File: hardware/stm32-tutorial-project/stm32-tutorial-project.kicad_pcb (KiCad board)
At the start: 2 copper layers, 7 parts, among them J2 10pin IDC SWD, U1 STM32G431CBTx

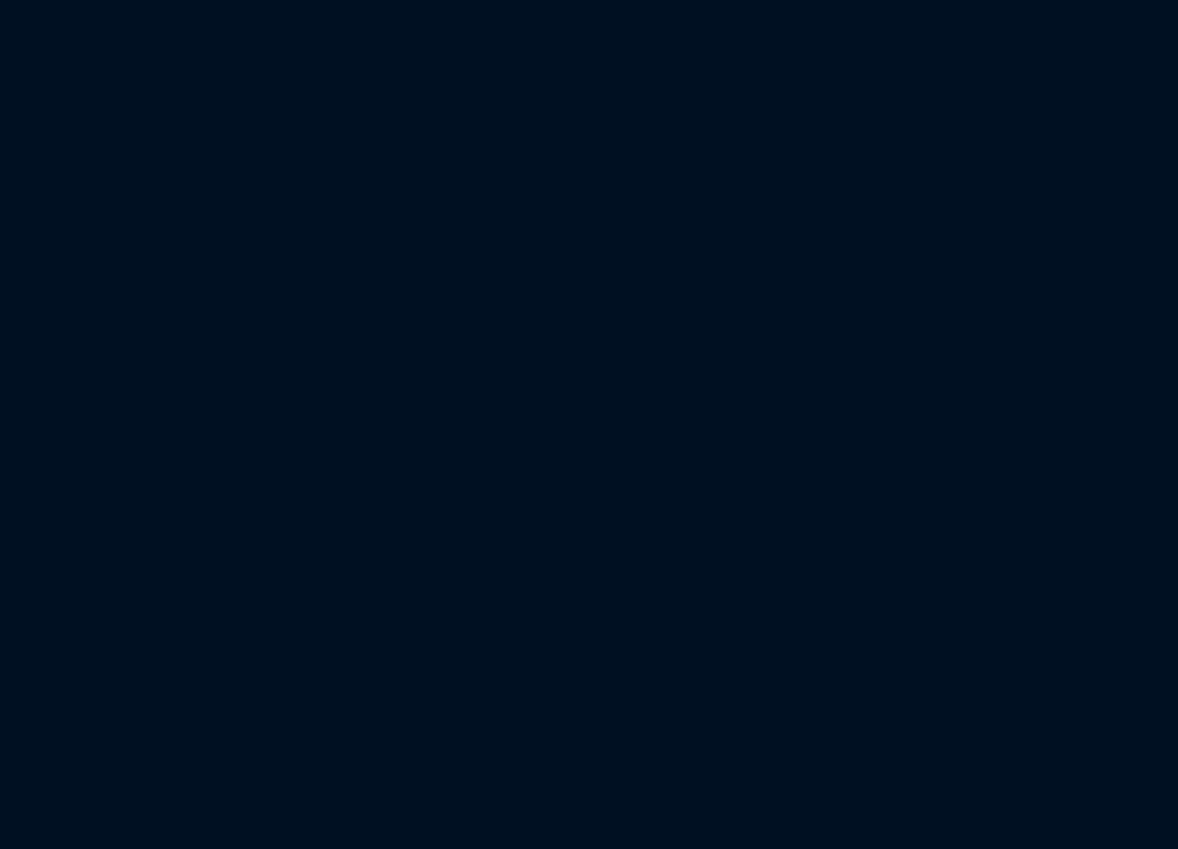
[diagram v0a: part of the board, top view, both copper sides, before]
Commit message: Add missing connectors, test points, and jumpers
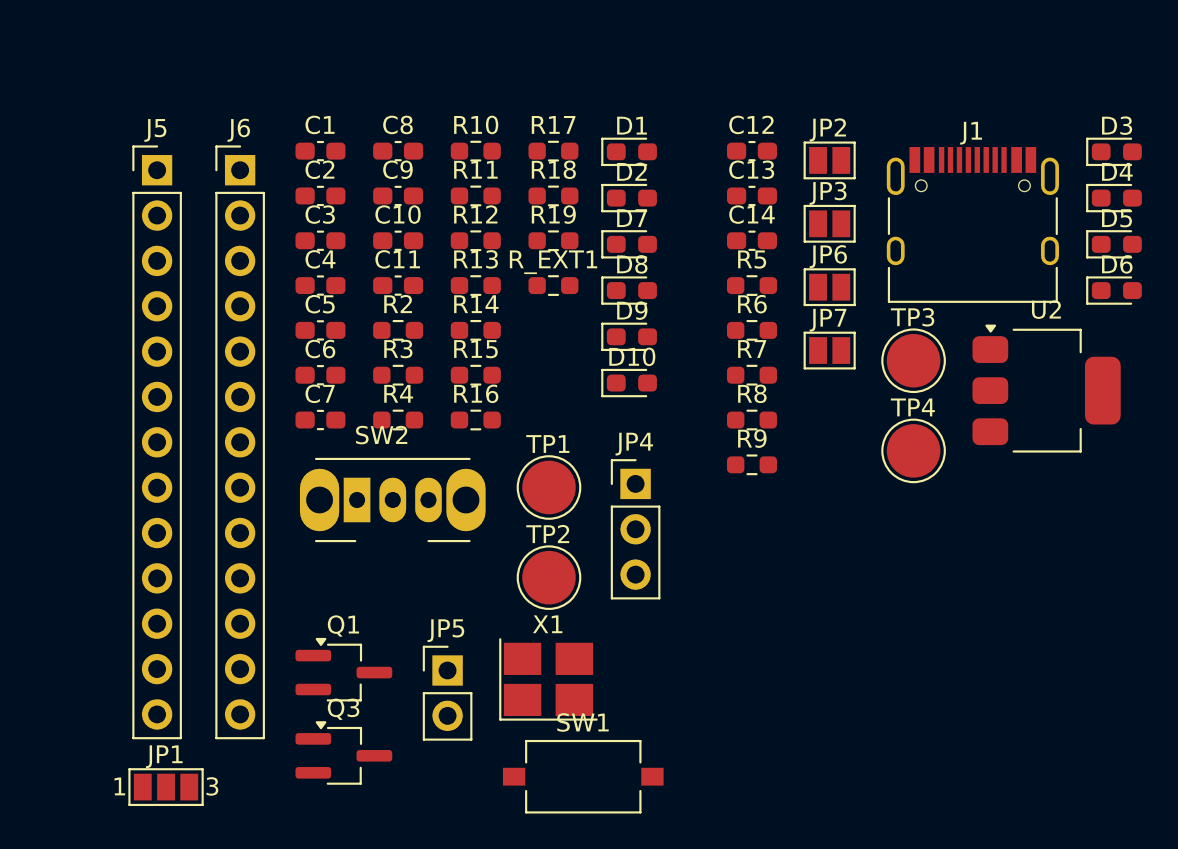
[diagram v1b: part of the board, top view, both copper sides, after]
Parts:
- added C1: 100n, Capacitor_SMD:C_0603_1608Metric_Pad1.08x0.95mm_HandSolder, F.Cu at (164.2, 111.1)
- added C10: 12pf, Capacitor_SMD:C_0603_1608Metric_Pad1.08x0.95mm_HandSolder, F.Cu at (168.5, 116.1)
- added C11: 100n, Capacitor_SMD:C_0603_1608Metric_Pad1.08x0.95mm_HandSolder, F.Cu at (168.5, 118.6)
- added C12: 10u, Capacitor_SMD:C_0603_1608Metric_Pad1.08x0.95mm_HandSolder, F.Cu at (188.3, 111.1)
- added C13: 10u, Capacitor_SMD:C_0603_1608Metric_Pad1.08x0.95mm_HandSolder, F.Cu at (188.3, 113.6)
- added C14: 22u, Capacitor_SMD:C_0603_1608Metric_Pad1.08x0.95mm_HandSolder, F.Cu at (188.3, 116.1)
- added C2: 1u, Capacitor_SMD:C_0603_1608Metric_Pad1.08x0.95mm_HandSolder, F.Cu at (164.2, 113.6)
- added C3: 4.7u, Capacitor_SMD:C_0603_1608Metric_Pad1.08x0.95mm_HandSolder, F.Cu at (164.2, 116.1)
- added C4: 100n, Capacitor_SMD:C_0603_1608Metric_Pad1.08x0.95mm_HandSolder, F.Cu at (164.2, 118.6)
- added C5: 100n, Capacitor_SMD:C_0603_1608Metric_Pad1.08x0.95mm_HandSolder, F.Cu at (164.2, 121.1)
- added C6: 100n, Capacitor_SMD:C_0603_1608Metric_Pad1.08x0.95mm_HandSolder, F.Cu at (164.2, 123.6)
- added C7: 10n, Capacitor_SMD:C_0603_1608Metric_Pad1.08x0.95mm_HandSolder, F.Cu at (164.2, 126.1)
- added C8: 1u, Capacitor_SMD:C_0603_1608Metric_Pad1.08x0.95mm_HandSolder, F.Cu at (168.5, 111.1)
- added C9: 12pf, Capacitor_SMD:C_0603_1608Metric_Pad1.08x0.95mm_HandSolder, F.Cu at (168.5, 113.6)
- added D1: LED, Diode_SMD:D_0603_1608Metric_Pad1.05x0.95mm_HandSolder, F.Cu at (181.6, 111.1)
- added D10: LED, Diode_SMD:D_0603_1608Metric_Pad1.05x0.95mm_HandSolder, F.Cu at (181.6, 124.1)
- added D2: LED, Diode_SMD:D_0603_1608Metric_Pad1.05x0.95mm_HandSolder, F.Cu at (181.6, 113.7)
- added D3: D_Schottky, Diode_SMD:D_0603_1608Metric_Pad1.05x0.95mm_HandSolder, F.Cu at (208.8, 111.1)
- added D4: D_Schottky, Diode_SMD:D_0603_1608Metric_Pad1.05x0.95mm_HandSolder, F.Cu at (208.8, 113.7)
- added D5: LED, Diode_SMD:D_0603_1608Metric_Pad1.05x0.95mm_HandSolder, F.Cu at (208.8, 116.3)
- added D6: LED, Diode_SMD:D_0603_1608Metric_Pad1.05x0.95mm_HandSolder, F.Cu at (208.8, 118.9)
- added D7: LED, Diode_SMD:D_0603_1608Metric_Pad1.05x0.95mm_HandSolder, F.Cu at (181.6, 116.3)
- added D8: LED, Diode_SMD:D_0603_1608Metric_Pad1.05x0.95mm_HandSolder, F.Cu at (181.6, 118.9)
- added D9: LED, Diode_SMD:D_0603_1608Metric_Pad1.05x0.95mm_HandSolder, F.Cu at (181.6, 121.5)
- added J1: USB_C_Receptacle_USB2.0_14P, Connector_USB:USB_C_Receptacle_HRO_TYPE-C-31-M-12, F.Cu at (200.7, 115.6)
- added J5: Conn_01x13, Connector_PinHeader_2.54mm:PinHeader_1x13_P2.54mm_Vertical, F.Cu at (155.0, 112.2)
- added J6: Conn_01x13, Connector_PinHeader_2.54mm:PinHeader_1x13_P2.54mm_Vertical, F.Cu at (159.7, 112.2)
- added JP1: VBAT_SLEC, Jumper:SolderJumper-3_P1.3mm_Open_Pad1.0x1.5mm_NumberLabels, F.Cu at (155.5, 146.7)
- added JP2: 5V_sense, Jumper:SolderJumper-2_P1.3mm_Open_Pad1.0x1.5mm, F.Cu at (192.7, 111.6)
- added JP3: Schottky_bypass, Jumper:SolderJumper-2_P1.3mm_Open_Pad1.0x1.5mm, F.Cu at (192.7, 115.2)
- added JP4: 5V_SLEC, Connector_PinHeader_2.54mm:PinHeader_1x03_P2.54mm_Vertical, F.Cu at (181.8, 129.7)
- added JP5: I2C_PULL_UPS_EN, Connector_PinHeader_2.54mm:PinHeader_1x02_P2.54mm_Vertical, F.Cu at (171.3, 140.2)
- added JP6: REG_OUT, Jumper:SolderJumper-2_P1.3mm_Open_Pad1.0x1.5mm, F.Cu at (192.7, 118.7)
- added JP7: REG_IN, Jumper:SolderJumper-2_P1.3mm_Open_Pad1.0x1.5mm, F.Cu at (192.7, 122.3)
- added Q1: NPN, Package_TO_SOT_SMD:TSOT-23_HandSoldering, F.Cu at (165.5, 140.3)
- added Q3: PNP, Package_TO_SOT_SMD:TSOT-23_HandSoldering, F.Cu at (165.5, 145.0)
- added R10: 500, Resistor_SMD:R_0603_1608Metric_Pad0.98x0.95mm_HandSolder, F.Cu at (172.9, 111.1)
- added R11: 500, Resistor_SMD:R_0603_1608Metric_Pad0.98x0.95mm_HandSolder, F.Cu at (172.9, 113.6)
- added R12: 500, Resistor_SMD:R_0603_1608Metric_Pad0.98x0.95mm_HandSolder, F.Cu at (172.9, 116.1)
- added R13: 1k, Resistor_SMD:R_0603_1608Metric_Pad0.98x0.95mm_HandSolder, F.Cu at (172.9, 118.6)
- added R14: 1k, Resistor_SMD:R_0603_1608Metric_Pad0.98x0.95mm_HandSolder, F.Cu at (172.9, 121.1)
- added R15: 500, Resistor_SMD:R_0603_1608Metric_Pad0.98x0.95mm_HandSolder, F.Cu at (172.9, 123.6)
- added R16: 10k, Resistor_SMD:R_0603_1608Metric_Pad0.98x0.95mm_HandSolder, F.Cu at (172.9, 126.1)
- added R17: 10k, Resistor_SMD:R_0603_1608Metric_Pad0.98x0.95mm_HandSolder, F.Cu at (177.2, 111.1)
- added R18: 4.7k, Resistor_SMD:R_0603_1608Metric_Pad0.98x0.95mm_HandSolder, F.Cu at (177.2, 113.6)
- added R19: 4.7k, Resistor_SMD:R_0603_1608Metric_Pad0.98x0.95mm_HandSolder, F.Cu at (177.2, 116.1)
- added R2: 500, Resistor_SMD:R_0603_1608Metric_Pad0.98x0.95mm_HandSolder, F.Cu at (168.5, 121.1)
- added R3: 10k, Resistor_SMD:R_0603_1608Metric_Pad0.98x0.95mm_HandSolder, F.Cu at (168.5, 123.6)
- added R4: 500, Resistor_SMD:R_0603_1608Metric_Pad0.98x0.95mm_HandSolder, F.Cu at (168.5, 126.1)
- added R5: 0, Resistor_SMD:R_0603_1608Metric_Pad0.98x0.95mm_HandSolder, F.Cu at (188.3, 118.6)
- added R6: 5.1k, Resistor_SMD:R_0603_1608Metric_Pad0.98x0.95mm_HandSolder, F.Cu at (188.3, 121.1)
- added R7: 5.1k, Resistor_SMD:R_0603_1608Metric_Pad0.98x0.95mm_HandSolder, F.Cu at (188.3, 123.6)
- added R8: 500, Resistor_SMD:R_0603_1608Metric_Pad0.98x0.95mm_HandSolder, F.Cu at (188.3, 126.1)
- added R9: 500, Resistor_SMD:R_0603_1608Metric_Pad0.98x0.95mm_HandSolder, F.Cu at (188.3, 128.7)
- added R_EXT1: 0, Resistor_SMD:R_0603_1608Metric_Pad0.98x0.95mm_HandSolder, F.Cu at (177.2, 118.6)
- added SW1: SW_Push, Button_Switch_SMD:SW_Tactile_SPST_NO_Straight_CK_PTS636Sx25SMTRLFS, F.Cu at (178.9, 146.1)
- added SW2: SW_Push_SPDT, Button_Switch_THT:SW_Slide_SPDT_Angled_CK_OS102011MA1Q, F.Cu at (166.2, 130.6)
- added TP1: DIGITAL_IO_1, TestPoint:TestPoint_Pad_D3.0mm, F.Cu at (177.0, 129.9)
- added TP2: DIGITAL_IO_2, TestPoint:TestPoint_Pad_D3.0mm, F.Cu at (177.0, 135.0)
- added TP3: VBUS, TestPoint:TestPoint_Pad_D3.0mm, F.Cu at (197.4, 122.8)
- added TP4: 5V, TestPoint:TestPoint_Pad_D3.0mm, F.Cu at (197.4, 127.9)
- added U2: AZ1117-3.3, Package_TO_SOT_SMD:SOT-223-3_TabPin2, F.Cu at (204.8, 124.5)
- added X1: Crystal_GND24, Crystal:Crystal_SMD_3225-4Pin_3.2x2.5mm_HandSoldering, F.Cu at (176.9, 140.7)
- D11: value SP0504BAHT -> SP0504BAHTG

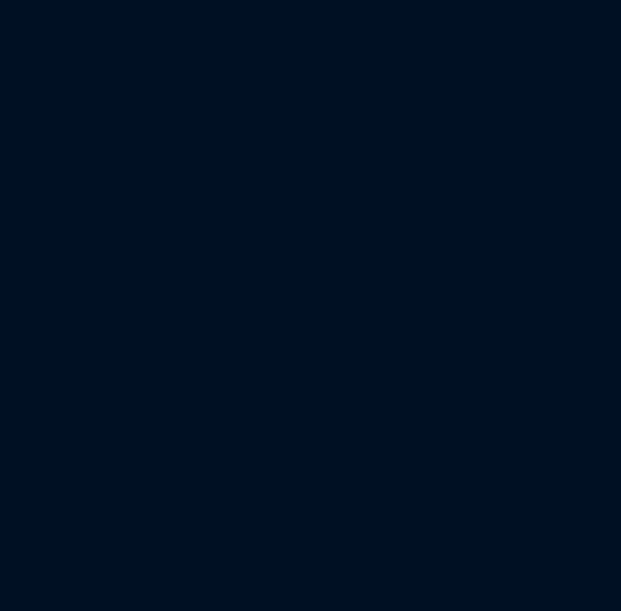
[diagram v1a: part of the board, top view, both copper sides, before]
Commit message: Correct remaining connectors, complete ratsnest now available
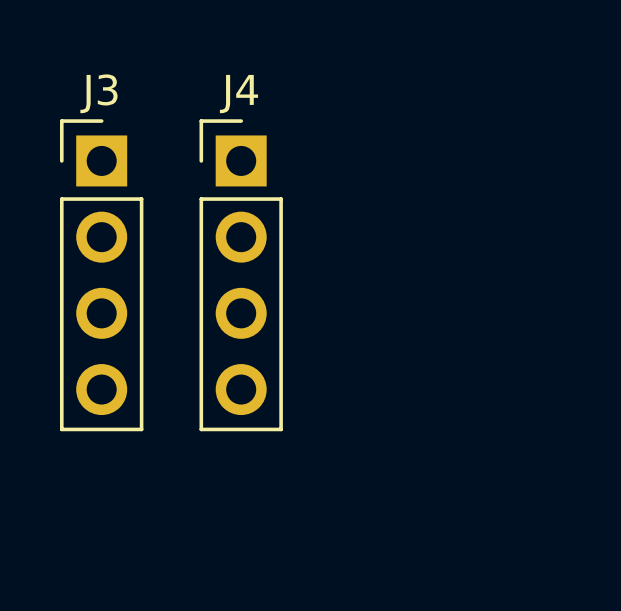
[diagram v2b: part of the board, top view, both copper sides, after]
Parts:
- added J3: Conn_01x04, Connector_PinHeader_2.54mm:PinHeader_1x04_P2.54mm_Vertical, F.Cu at (105.3, 77.4)
- added J4: Conn_01x04, Connector_PinHeader_2.54mm:PinHeader_1x04_P2.54mm_Vertical, F.Cu at (110.0, 77.4)

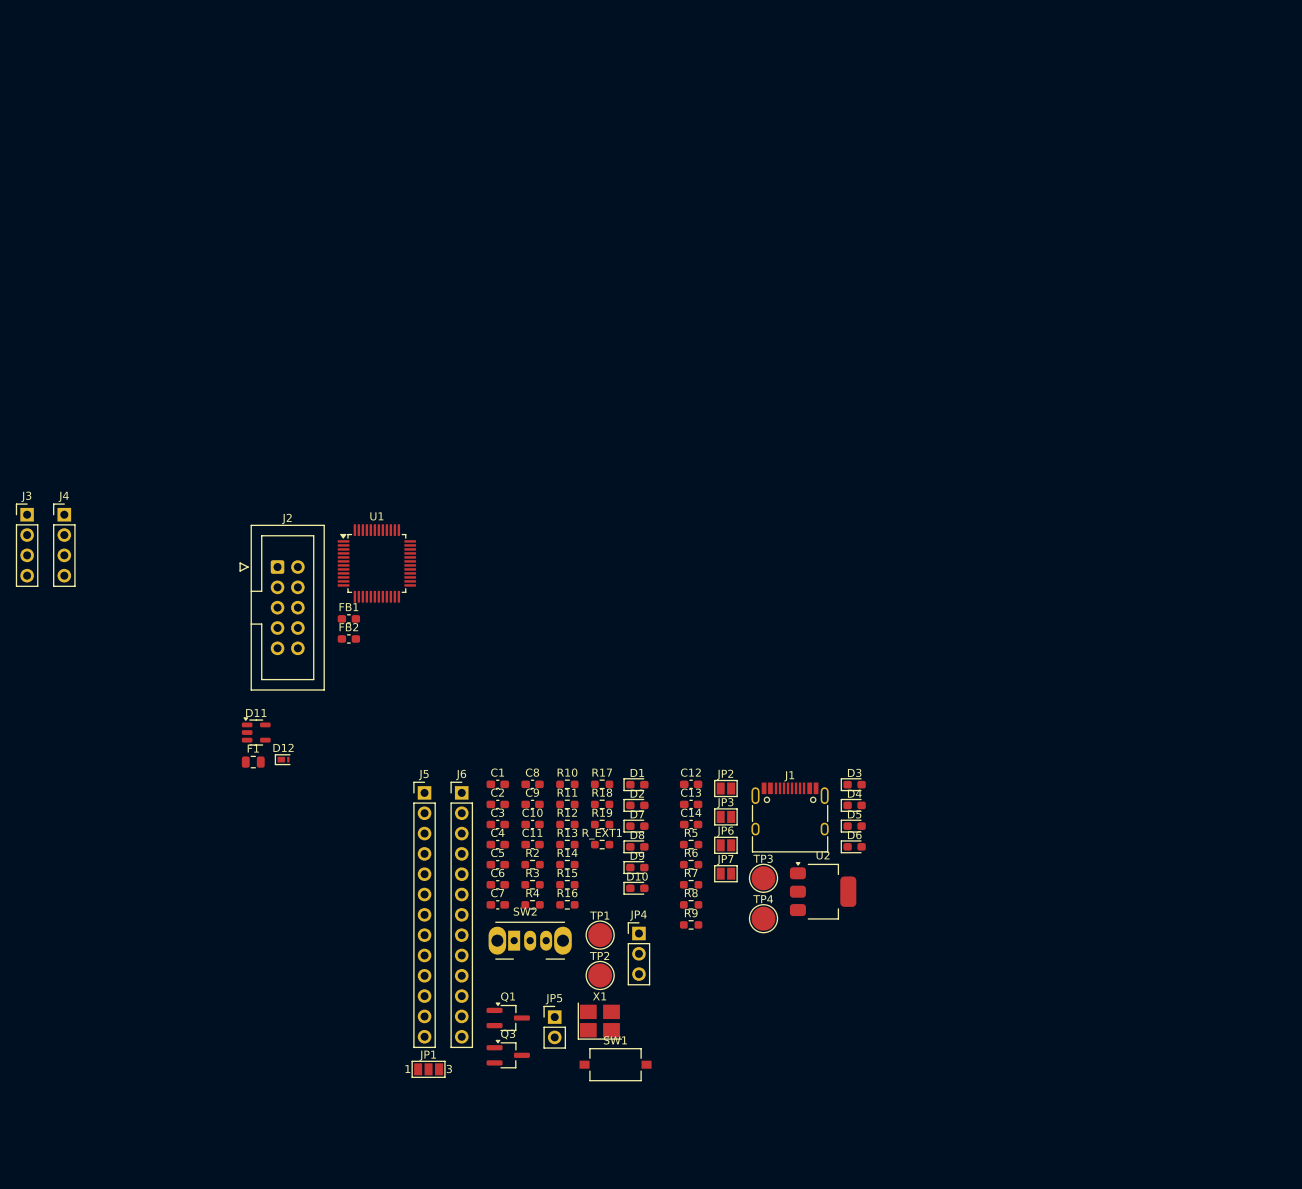
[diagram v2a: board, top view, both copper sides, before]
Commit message: Break ratsnest into functional sections
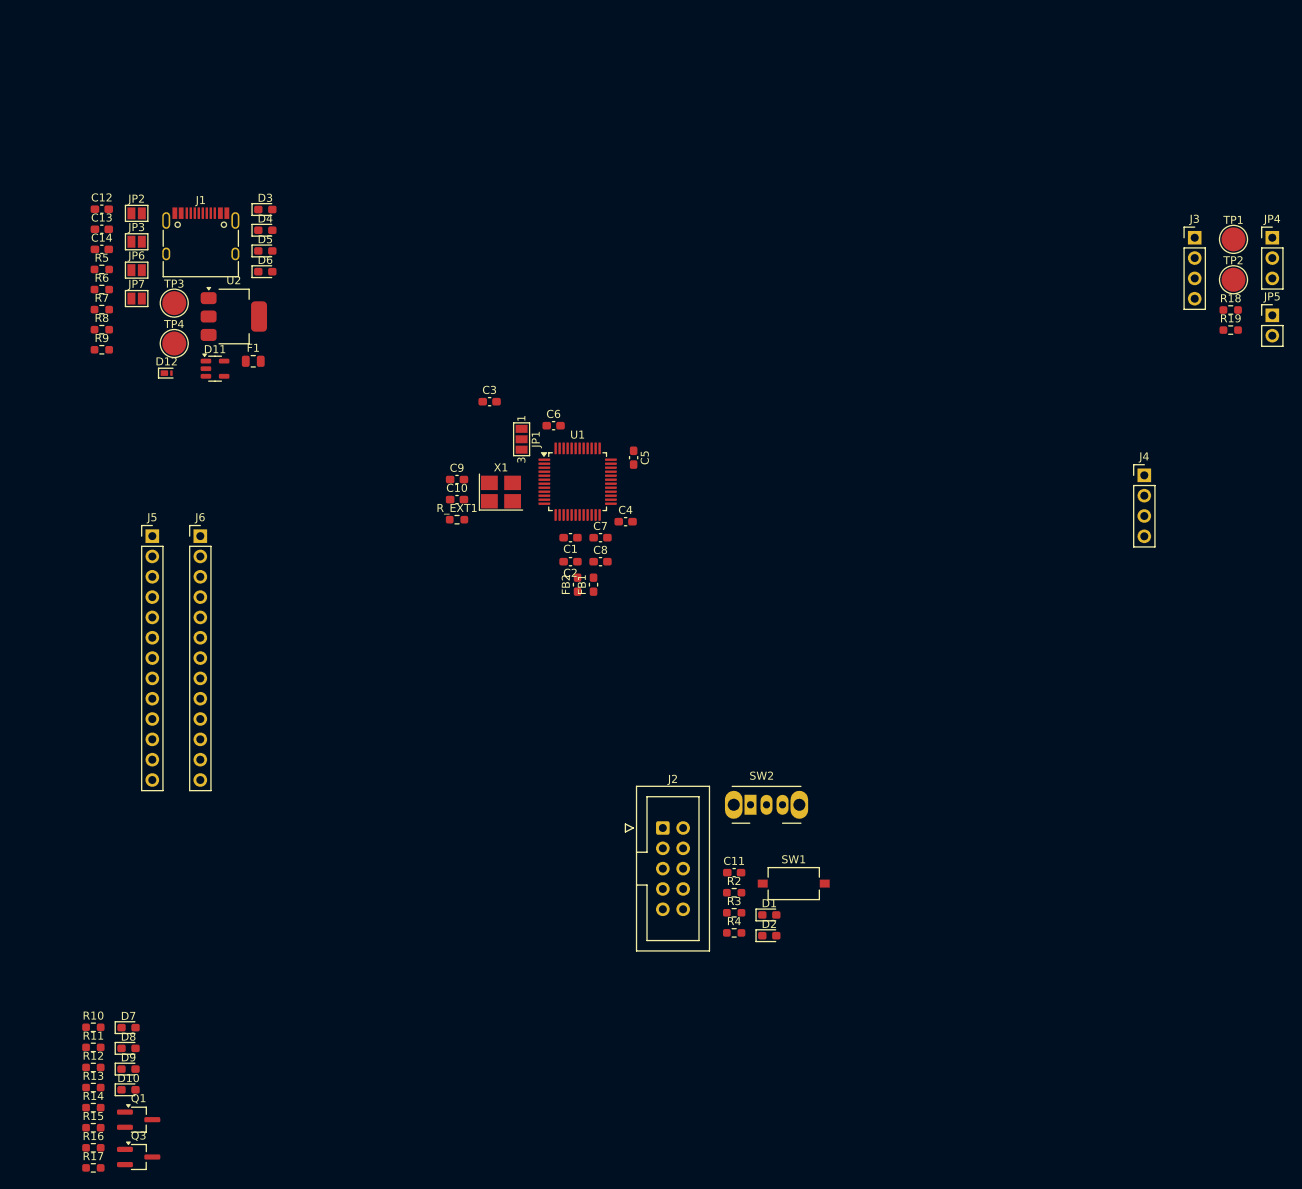
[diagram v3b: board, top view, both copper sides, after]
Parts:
- moved J3 150.0 mm to (251.3, 42.8)
- moved J4 135.1 mm to (245.0, 72.5)
- moved JP5 125.5 mm to (261.0, 52.5)
- moved JP4 117.6 mm to (261.0, 42.8)
- moved TP1 117.6 mm to (256.1, 43.0)
- moved TP2 117.6 mm to (256.1, 48.0)
- moved C14 102.9 mm to (114.7, 44.2)
- moved D3 102.9 mm to (135.1, 39.2)
- moved D4 102.9 mm to (135.1, 41.8)
- moved D5 102.9 mm to (135.1, 44.4)
- moved J1 102.9 mm to (127.1, 43.7)
- moved R6 102.9 mm to (114.7, 49.2)
- moved R7 102.9 mm to (114.7, 51.7)
- moved R9 102.9 mm to (114.7, 56.8)
- moved TP3 102.9 mm to (123.7, 50.9)
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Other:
- board text added: "Analogue sensor"
- board text added: "Digital sensor"
- board text added: "LEDs"
- board text added: "MCU"
- board text added: "Pins"
- board text added: "Power"
- board text added: "Programming/boot"
